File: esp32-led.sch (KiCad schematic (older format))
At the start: 10 parts, among them J1 LED Connector, J2 USB4125-GF-A_REVA2, J3 LED Connector, U1 SN74AHCT125D, U2 ESP32_NODEMCU

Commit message: Fixed issues, added gerber files
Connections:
- net +5V: now also J3.3 (Pin_3); no longer J3.1 (Pin_1)
- net GND: now also J3.1 (Pin_1); no longer J3.3 (Pin_3)
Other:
- moved on the sheet: C1, J1, J3
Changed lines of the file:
@@
 Wire Notes Line
 	3450 3600 950  3600
-Text GLabel 1600 2450 0    50   Input ~ 0
+Text GLabel 2100 2650 0    50   Input ~ 0
 DATA
 $Comp
 L Connector:Conn_01x03_Male J1
 U 1 1 62EB48AB
-P 2850 2250
-F 0 "J1" H 2822 2182 50  0000 R CNN
-F 1 "LED Connector" H 2822 2273 50  0000 R CNN
-F 2 "Connector_PinHeader_2.54mm:PinHeader_1x03_P2.54mm_Vertical" H 2850 2250 50  0001 C CNN
-F 3 "~" H 2850 2250 50  0001 C CNN
-	1    2850 2250
+P 2800 2300
+F 0 "J1" H 2772 2232 50  0000 R CNN
+F 1 "LED Connector" H 2772 2323 50  0000 R CNN
+F 2 "Connector_PinHeader_2.54mm:PinHeader_1x03_P2.54mm_Vertical" H 2800 2300 50  0001 C CNN
+F 3 "~" H 2800 2300 50  0001 C CNN
+	1    2800 2300
 	-1   0    0    1
 $EndComp
@@
 L Device:CP C1
 U 1 1 62EB16DE
-P 2050 3150
-F 0 "C1" H 2168 3196 50  0000 L CNN
-F 1 "CP" H 2168 3105 50  0000 L CNN
-F 2 "Capacitor_THT:CP_Radial_D10.0mm_P5.00mm" H 2088 3000 50  0001 C CNN
-F 3 "~" H 2050 3150 50  0001 C CNN
-	1    2050 3150
+P 1400 2400
+F 0 "C1" H 1518 2446 50  0000 L CNN
+F 1 "CP" H 1518 2355 50  0000 L CNN
+F 2 "Capacitor_THT:CP_Radial_D10.0mm_P5.00mm" H 1438 2250 50  0001 C CNN
+F 3 "~" H 1400 2400 50  0001 C CNN
+	1    1400 2400
 	1    0    0    -1
 $EndComp
@@
 L power:+5V #PWR01
 U 1 1 62EB0400
-P 1200 2450
-F 0 "#PWR01" H 1200 2300 50  0001 C CNN
-F 1 "+5V" H 1215 2623 50  0000 C CNN
-F 2 "" H 1200 2450 50  0001 C CNN
-F 3 "" H 1200 2450 50  0001 C CNN
-	1    1200 2450
+P 2000 2200
+F 0 "#PWR01" H 2000 2050 50  0001 C CNN
+F 1 "+5V" H 2015 2373 50  0000 C CNN
+F 2 "" H 2000 2200 50  0001 C CNN
+F 3 "" H 2000 2200 50  0001 C CNN
+	1    2000 2200
 	0    -1   -1   0
 $EndComp
@@
 L power:GND #PWR02
 U 1 1 62EAF6FE
-P 1900 2450
-F 0 "#PWR02" H 1900 2200 50  0001 C CNN
-F 1 "GND" H 1905 2277 50  0000 C CNN
-F 2 "" H 1900 2450 50  0001 C CNN
-F 3 "" H 1900 2450 50  0001 C CNN
-	1    1900 2450
+P 1950 2750
+F 0 "#PWR02" H 1950 2500 50  0001 C CNN
+F 1 "GND" H 1955 2577 50  0000 C CNN
+F 2 "" H 1950 2750 50  0001 C CNN
+F 3 "" H 1950 2750 50  0001 C CNN
+	1    1950 2750
 	0    1    1    0
 $EndComp
@@
 L Connector:Conn_01x03_Male J3
 U 1 1 62E912D3
-P 2850 2650
-F 0 "J3" H 2822 2582 50  0000 R CNN
-F 1 "LED Connector" H 2822 2673 50  0000 R CNN
-F 2 "Connector_PinHeader_2.54mm:PinHeader_1x03_P2.54mm_Vertical" H 2850 2650 50  0001 C CNN
-F 3 "~" H 2850 2650 50  0001 C CNN
-	1    2850 2650
+P 2800 2650
+F 0 "J3" H 2772 2582 50  0000 R CNN
+F 1 "LED Connector" H 2772 2673 50  0000 R CNN
+F 2 "Connector_PinHeader_2.54mm:PinHeader_1x03_P2.54mm_Vertical" H 2800 2650 50  0001 C CNN
+F 3 "~" H 2800 2650 50  0001 C CNN
+	1    2800 2650
 	-1   0    0    1
 $EndComp
-Wire Wire Line
-	1900 2450 2400 2450
-Wire Wire Line
-	2400 2450 2400 2350
-Wire Wire Line
-	2400 2350 2650 2350
-Wire Wire Line
-	2400 2450 2400 2550
-Wire Wire Line
-	2400 2550 2650 2550
-Connection ~ 2400 2450
-Wire Wire Line
-	1600 2450 1650 2450
-Wire Wire Line
-	1650 2450 1650 2250
-Wire Wire Line
-	1650 2250 2650 2250
-Wire Wire Line
-	1650 2450 1650 2650
-Wire Wire Line
-	1650 2650 2650 2650
-Connection ~ 1650 2450
-Wire Wire Line
-	1200 2450 1200 2150
-Wire Wire Line
-	1200 2450 1200 2750
-Wire Wire Line
-	1200 2750 2650 2750
-Connection ~ 1200 2450
-Wire Wire Line
-	1200 2150 2650 2150
 $Comp
 L power:+5V #PWR09
 U 1 1 62ED22FC
-P 2050 3000
-F 0 "#PWR09" H 2050 2850 50  0001 C CNN
-F 1 "+5V" H 2065 3173 50  0000 C CNN
-F 2 "" H 2050 3000 50  0001 C CNN
-F 3 "" H 2050 3000 50  0001 C CNN
-	1    2050 3000
+P 1400 2250
+F 0 "#PWR09" H 1400 2100 50  0001 C CNN
+F 1 "+5V" H 1415 2423 50  0000 C CNN
+F 2 "" H 1400 2250 50  0001 C CNN
+F 3 "" H 1400 2250 50  0001 C CNN
+	1    1400 2250
 	1    0    0    -1
 $EndComp
@@
 L power:GND #PWR010
 U 1 1 62ED32C8
-P 2050 3300
-F 0 "#PWR010" H 2050 3050 50  0001 C CNN
-F 1 "GND" H 2055 3127 50  0000 C CNN
-F 2 "" H 2050 3300 50  0001 C CNN
-F 3 "" H 2050 3300 50  0001 C CNN
-	1    2050 3300
+P 1400 2550
+F 0 "#PWR010" H 1400 2300 50  0001 C CNN
+F 1 "GND" H 1405 2377 50  0000 C CNN
+F 2 "" H 1400 2550 50  0001 C CNN
+F 3 "" H 1400 2550 50  0001 C CNN
+	1    1400 2550
 	1    0    0    -1
 $EndComp
@@
 Wire Notes Line
 	950  1800 950  3600
+Wire Wire Line
+	2600 2200 2150 2200
+Wire Wire Line
+	2150 2200 2150 2550
+Wire Wire Line
+	2150 2550 2600 2550
+Wire Wire Line
+	2150 2200 2000 2200
+Connection ~ 2150 2200
+Wire Wire Line
+	2600 2300 2350 2300
+Wire Wire Line
+	2350 2300 2350 2650
+Wire Wire Line
+	2350 2650 2600 2650
+Wire Wire Line
+	2100 2650 2350 2650
+Connection ~ 2350 2650
+Wire Wire Line
+	2600 2400 2450 2400
+Wire Wire Line
+	2450 2400 2450 2750
+Wire Wire Line
+	2450 2750 2600 2750
+Wire Wire Line
+	2450 2750 1950 2750
+Connection ~ 2450 2750
 $EndSCHEMATC

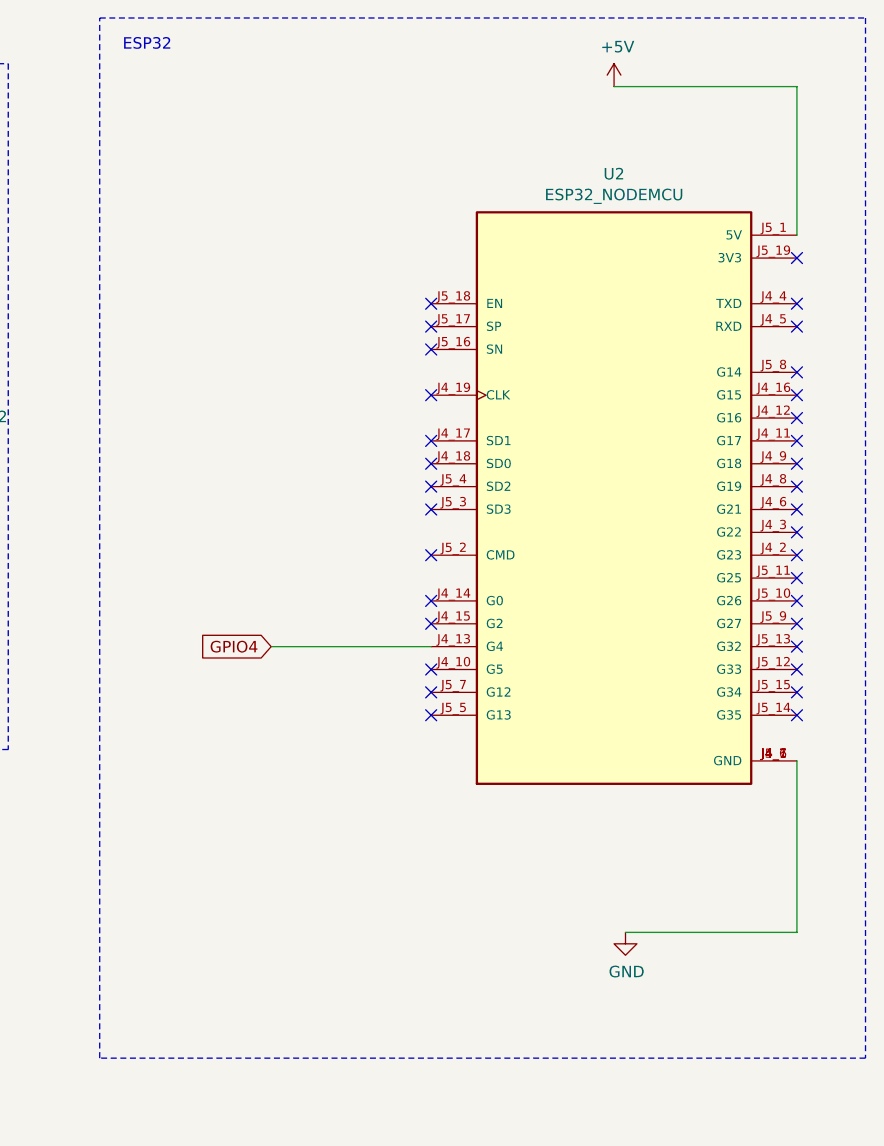
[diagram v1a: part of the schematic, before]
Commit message: Chamged wrong esp32 footprint
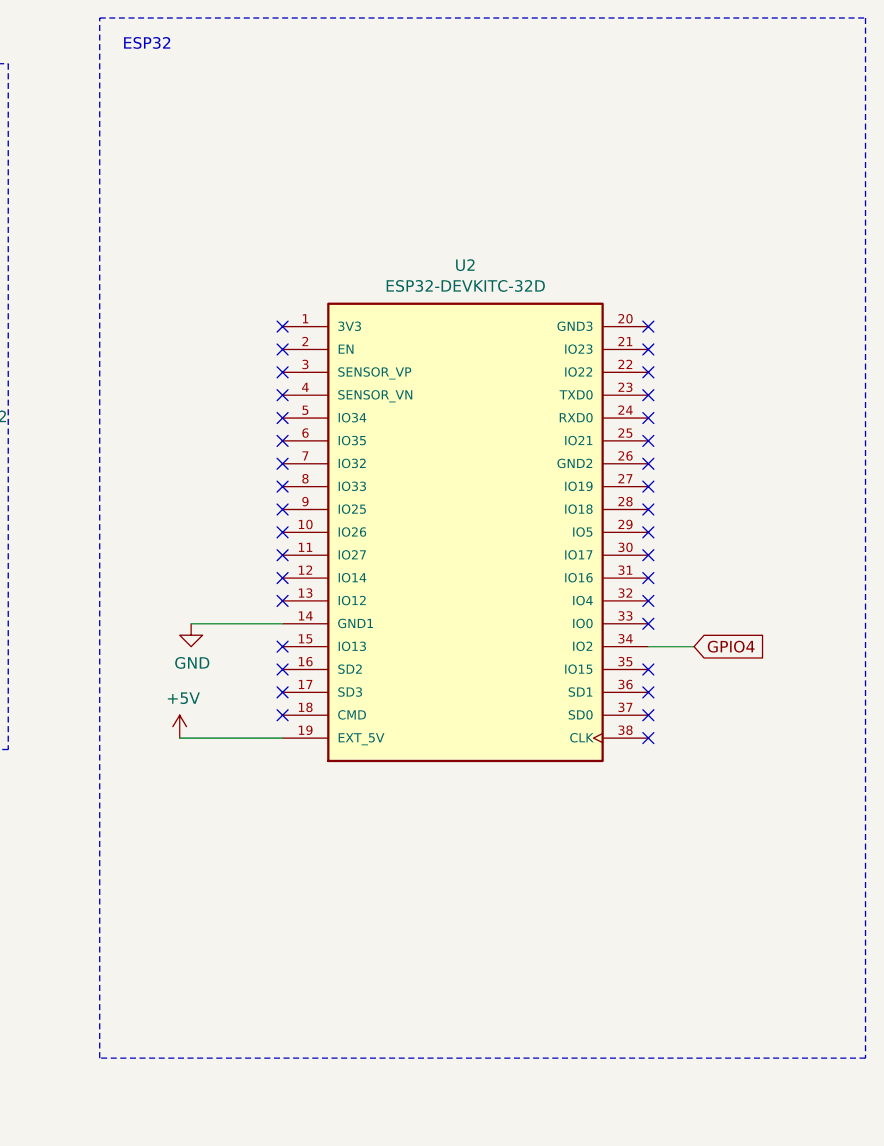
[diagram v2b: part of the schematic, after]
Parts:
- removed U2: ESP32_NODEMCU, ESP32_NODEMCU:MODULE_ESP32_NODEMCU, symbol ESP32_NODEMCU:ESP32_NODEMCU
- added U2: ESP32-DEVKITC-32D, ESP32-DEVKITC-32D:MODULE_ESP32-DEVKITC-32D, symbol ESP32-DEVKITC-32D:ESP32-DEVKITC-32D
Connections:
- net +5V: now also U2.19 (EXT_5V)
- net GND: now also U2.14 (GND1)
- net GPIO4: now also U2.34 (IO2)
- no-connect marks 39 -> 41
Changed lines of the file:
@@
 Wire Notes Line
 	10300 650  10300 5200
-Wire Wire Line
-	8400 3400 7700 3400
-Text GLabel 7700 3400 0    50   Input ~ 0
+Text GLabel 9550 3400 2    50   Input ~ 0
 GPIO4
-Wire Wire Line
-	10000 4650 9250 4650
-Wire Wire Line
-	10000 3900 10000 4650
 $Comp
 L power:GND #PWR08
 U 1 1 62EA1CA8
-P 9250 4650
-F 0 "#PWR08" H 9250 4400 50  0001 C CNN
-F 1 "GND" H 9255 4477 50  0000 C CNN
-F 2 "" H 9250 4650 50  0001 C CNN
-F 3 "" H 9250 4650 50  0001 C CNN
-	1    9250 4650
-	1    0    0    -1
-$EndComp
-NoConn ~ 10000 1700
-NoConn ~ 10000 1900
-NoConn ~ 10000 2000
-NoConn ~ 10000 2200
-NoConn ~ 10000 2300
-NoConn ~ 10000 2400
-NoConn ~ 10000 2500
-NoConn ~ 10000 2600
-NoConn ~ 10000 2700
-NoConn ~ 10000 2800
-NoConn ~ 10000 2900
-NoConn ~ 10000 3000
-NoConn ~ 10000 3100
-NoConn ~ 10000 3200
-NoConn ~ 10000 3300
-NoConn ~ 10000 3400
-NoConn ~ 10000 3500
-NoConn ~ 10000 3600
-NoConn ~ 10000 3700
-NoConn ~ 8400 3700
-NoConn ~ 8400 3600
-NoConn ~ 8400 3500
-NoConn ~ 8400 3300
-NoConn ~ 8400 3200
-NoConn ~ 8400 3000
-NoConn ~ 8400 2800
-NoConn ~ 8400 2700
-NoConn ~ 8400 2600
-NoConn ~ 8400 2500
-NoConn ~ 8400 2300
-NoConn ~ 8400 2100
-NoConn ~ 8400 2000
-NoConn ~ 8400 1900
-$Comp
-L ESP32_NODEMCU:ESP32_NODEMCU U2
-U 1 1 62E9349D
-P 9200 2700
-F 0 "U2" H 9200 4067 50  0000 C CNN
-F 1 "ESP32_NODEMCU" H 9200 3976 50  0000 C CNN
-F 2 "ESP32_NODEMCU:MODULE_ESP32_NODEMCU" H 9200 2700 50  0001 L BNN
-F 3 "" H 9200 2700 50  0001 L BNN
-F 4 "6.6 mm" H 9200 2700 50  0001 L BNN "MAXIMUM_PACKAGE_HEIGHT"
-F 5 "Espressif" H 9200 2700 50  0001 L BNN "MANUFACTURER"
-F 6 "Manufacturer Recommendations" H 9200 2700 50  0001 L BNN "STANDARD"
-	1    9200 2700
-	1    0    0    -1
-$EndComp
-Wire Wire Line
-	10000 950  10000 1600
-Wire Wire Line
-	9200 950  10000 950
+P 7350 3300
+F 0 "#PWR08" H 7350 3050 50  0001 C CNN
+F 1 "GND" H 7355 3127 50  0000 C CNN
+F 2 "" H 7350 3300 50  0001 C CNN
+F 3 "" H 7350 3300 50  0001 C CNN
+	1    7350 3300
+	1    0    0    -1
+$EndComp
 $Comp
 L power:+5V #PWR07
 U 1 1 62E9556F
-P 9200 950
-F 0 "#PWR07" H 9200 800 50  0001 C CNN
-F 1 "+5V" H 9215 1123 50  0000 C CNN
-F 2 "" H 9200 950 50  0001 C CNN
-F 3 "" H 9200 950 50  0001 C CNN
-	1    9200 950
+P 7300 3800
+F 0 "#PWR07" H 7300 3650 50  0001 C CNN
+F 1 "+5V" H 7315 3973 50  0000 C CNN
+F 2 "" H 7300 3800 50  0001 C CNN
+F 3 "" H 7300 3800 50  0001 C CNN
+	1    7300 3800
 	1    0    0    -1
 $EndComp
@@
 	2450 2750 1950 2750
 Connection ~ 2450 2750
+$Comp
+L ESP32-DEVKITC-32D:ESP32-DEVKITC-32D U2
+U 1 1 630123E6
+P 8550 2900
+F 0 "U2" H 8550 4067 50  0000 C CNN
+F 1 "ESP32-DEVKITC-32D" H 8550 3976 50  0000 C CNN
+F 2 "ESP32-DEVKITC-32D:MODULE_ESP32-DEVKITC-32D" H 8550 2900 50  0001 L BNN
+F 3 "" H 8550 2900 50  0001 L BNN
+F 4 "Espressif Systems" H 8550 2900 50  0001 L BNN "MANUFACTURER"
+F 5 "4" H 8550 2900 50  0001 L BNN "PARTREV"
+	1    8550 2900
+	1    0    0    -1
+$EndComp
+Wire Wire Line
+	7750 3800 7300 3800
+Wire Wire Line
+	7750 3300 7350 3300
+Wire Wire Line
+	9350 3400 9550 3400
+NoConn ~ 9350 2000
+NoConn ~ 9350 2100
+NoConn ~ 9350 2200
+NoConn ~ 9350 2300
+NoConn ~ 9350 2400
+NoConn ~ 9350 2500
+NoConn ~ 9350 2600
+NoConn ~ 9350 2700
+NoConn ~ 9350 2800
+NoConn ~ 9350 2900
+NoConn ~ 9350 3000
+NoConn ~ 9350 3100
+NoConn ~ 9350 3200
+NoConn ~ 9350 3300
+NoConn ~ 9350 3500
+NoConn ~ 9350 3600
+NoConn ~ 9350 3700
+NoConn ~ 9350 3800
+NoConn ~ 7750 3700
+NoConn ~ 7750 3600
+NoConn ~ 7750 3500
+NoConn ~ 7750 3400
+NoConn ~ 7750 2000
+NoConn ~ 7750 2100
+NoConn ~ 7750 2200
+NoConn ~ 7750 2300
+NoConn ~ 7750 2400
+NoConn ~ 7750 2500
+NoConn ~ 7750 2600
+NoConn ~ 7750 2700
+NoConn ~ 7750 2800
+NoConn ~ 7750 2900
+NoConn ~ 7750 3000
+NoConn ~ 7750 3100
+NoConn ~ 7750 3200
 $EndSCHEMATC
